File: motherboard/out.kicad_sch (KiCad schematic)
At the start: 72 parts, among them J301 BNC, J302 BNC, J303 BNC, J304 BNC, J305 BNC, J306 BNC, U301 LMH6609, U302 LMH6609, U303 LMH6609, U304 LMH6609, U305 LMH6609, U306 LMH6609

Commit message: add ESD protection (14V TVS)
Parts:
- added D301, D302, D303, D304, D305, D306: 14V TVS, Capacitor_SMD:C_0402_1005Metric, symbol #SRS:3_ICs/3-02609
- L301, L302, L303, L304, L305, L306: value 1.5UH -> 1.5μH
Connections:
- net GND: now also D301.2 (ANODE), D302.2 (ANODE), D303.2 (ANODE), D304.2 (ANODE), D305.2 (ANODE), D306.2 (ANODE)
- net OUT1: now also D301.1 (CATHODE)
- net OUT2: now also D302.1 (CATHODE)
- net OUT3: now also D303.1 (CATHODE)
- net OUT4: now also D304.1 (CATHODE)
- net OUT5: now also D305.1 (CATHODE)
- net OUT6: now also D306.1 (CATHODE)
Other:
- note added: "ESD PROTECTION"
- moved on the sheet: J301, J302, J303, J304, J305, J306

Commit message: update OCXO bead to SMB2.5R-2 (higher current)
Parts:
- D301, D302, D303, D304, D305, D306: Footprint Modified By assignment_engine -> (none); Footprint Modified Timestamp 2025-10-13 21:00:11 -0800 -> (none); Imported from Altium 2025-07-21 -> (none); JLCPCB (none) -> C7473167; Manf Littelfuse Inc. -> (none); Price 0.15 -> (none); Qty In Stock 9228 -> (none); Recommended Y -> (none); Symbol DISC_SRS:DIODE-TVS -> (none); Symbol Modified By assignment_engine -> (none); Symbol Modified Timestamp 2025-10-13 21:00:11 -0800 -> (none); Tempco (none) -> (none); Used In FS740,FS752 -> (none)

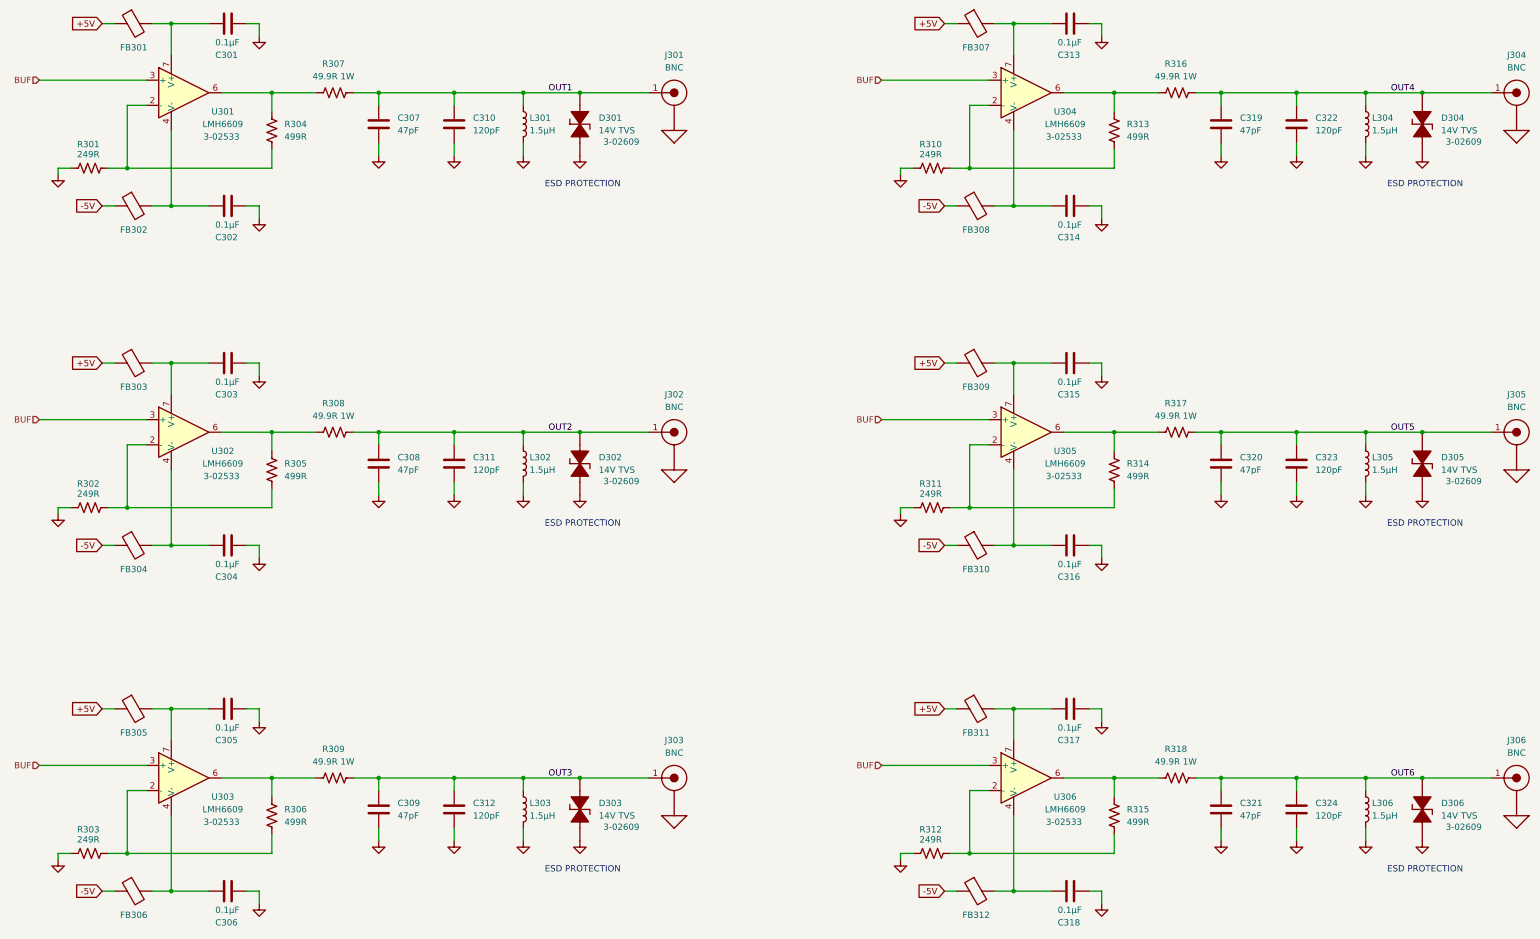
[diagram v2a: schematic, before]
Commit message: make FREQ_CTL filter cap an NP0 part
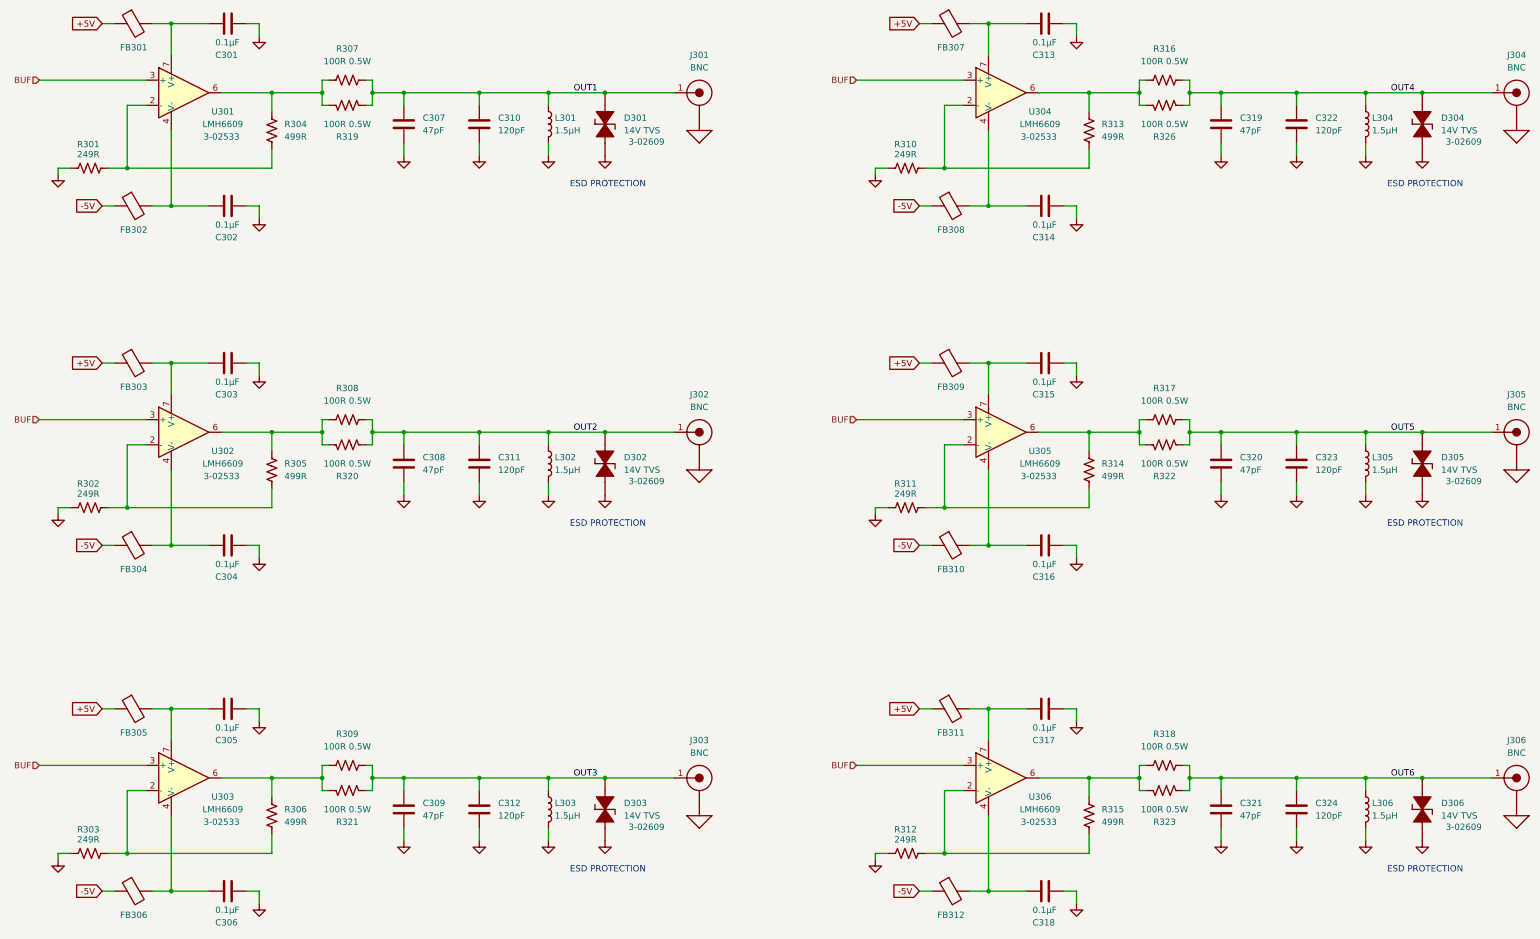
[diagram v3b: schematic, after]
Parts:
- removed R307, R308, R309, R316, R317, R318: 49.9R 1W, Resistor_SMD:R_2512_6332Metric, symbol #SRS:4_Resistors/4-02510
- added R307, R308, R309, R316, R317, R318, R319, R320, R321, R322, R323, R326: 100R 0.5W, Resistor_SMD:R_1206_3216Metric, symbol #SRS:4_Resistors/4-02555
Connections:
- net OUT1: now also R307.2, R319.2
- net OUT2: now also R308.2, R320.2
- net OUT3: now also R309.2, R321.2
- net OUT4: now also R316.2, R326.2
- net OUT5: now also R317.2, R322.2
- net OUT6: now also R318.2, R323.2
- net at R315.1, U306.6: now also R318.1, R323.1
- net at R306.1, U303.6: now also R309.1, R321.1
- net at R313.1, U304.6: now also R316.1, R326.1
- net at R305.1, U302.6: now also R308.1, R320.1
- net at R314.1, U305.6: now also R317.1, R322.1
- net at R304.1, U301.6: now also R307.1, R319.1
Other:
- moved on the sheet: C307, C308, C309, C310, C311, C312, C313, C314, C315, C316, C317, C318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
